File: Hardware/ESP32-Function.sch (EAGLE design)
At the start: 34 parts, among them J1 MICROMOD_STANDARD, Q2 MBT3904DW1T1, U1 EEPROM, U2 ESP-WROOM-3232D-NARROW, U3 3.3V, U4 CP210X

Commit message: Moves to 0603 components where able, adds silk, fixes traces affected by move to 0603
* removes wire stubs
* Fixes random air wires
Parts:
- removed C5: 0.1uF, SparkFun-Capacitors:0.1UF-0402T-16V-10%
- C1: device SparkFun-Capacitors:0.1UF-0402T-16V-10% -> SparkFun-Capacitors:0.1UF-0603-25V-(+80/-20%)
- C4: value 0.1uF -> 1.0uF; device SparkFun-Capacitors:0.1UF-0402T-16V-10% -> SparkFun-Capacitors:1.0UF-0603-16V-10%
- C6: device SparkFun-Capacitors:1.0UF-0402T-16V-10% -> SparkFun-Capacitors:1.0UF-0603-16V-10%
- D1: device SparkFun-MicroMod-Function:LED-0603_RIGHT_ANGLE -> SparkFun-LED:LED-RED0603
- R1, R17, R18, R2: device SparkFun-Resistors:10KOHM-0402T-1/16W-1% -> SparkFun-Resistors:10KOHM-0603-1/10W-1%
- R12: device SparkFun-Resistors:100KOHM-0402T-1/16W-1% -> SparkFun-Resistors:100KOHM-0603-1/10W-1%
- R3, R4: device SparkFun-Resistors:5.1KOHM-0402T-1/16W-1% -> SparkFun-Resistors:5.1KOHM5.1KOHM-0603-1/10W-1%
- R5: device SparkFun-Resistors:22KOHM-0402_TIGHT-1/10W-1% -> SparkFun-Resistors:22KOHM-0603-1/10W-1%
- R6: device SparkFun-Resistors:33KOHM-0402T-1/16W-1% -> SparkFun-Resistors:33KOHM-0603-1/10W-1%
- R7: device SparkFun-Resistors:1KOHM-0402T-1/16W-1% -> SparkFun-Resistors:1KOHM-0603-1/10W-1%
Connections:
- net 3.3V: no longer C5.2
- net GND: no longer C5.1
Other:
- note added: "v10"
- note removed: "v01"
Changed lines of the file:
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@@
 <?xml version="1.0" encoding="utf-8"?>
 <!DOCTYPE eagle SYSTEM "eagle.dtd">
-<eagle version="9.5.1">
+<eagle version="9.6.2">
 <drawing>
 <settings>
@@
 <part name="FD2" library="SparkFun-Aesthetics" deviceset="FIDUCIAL" device="1X2"/>
 <part name="FD4" library="SparkFun-Aesthetics" deviceset="FIDUCIAL" device="1X2"/>
-<part name="R17" library="SparkFun-Resistors" deviceset="10KOHM" device="-0402T-1/16W-1%" value="10k"/>
-<part name="R18" library="SparkFun-Resistors" deviceset="10KOHM" device="-0402T-1/16W-1%" value="10k"/>
+<part name="R17" library="SparkFun-Resistors" deviceset="10KOHM" device="-0603-1/10W-1%" value="10k"/>
+<part name="R18" library="SparkFun-Resistors" deviceset="10KOHM" device="-0603-1/10W-1%" value="10k"/>
 <part name="Q2" library="SparkFun-DiscreteSemi" deviceset="TRANS_NPN_DUAL" device="-MBT3904DW1T1" value="MBT3904DW1T1"/>
-<part name="C4" library="SparkFun-Capacitors" deviceset="0.1UF" device="-0402T-16V-10%" value="0.1uF"/>
+<part name="C4" library="SparkFun-Capacitors" deviceset="1.0UF" device="-0603-16V-10%" value="1.0uF"/>
 <part name="GND11" library="SparkFun-PowerSymbols" deviceset="GND" device=""/>
-<part name="C5" library="SparkFun-Capacitors" deviceset="0.1UF" device="-0402T-16V-10%" value="0.1uF"/>
-<part name="GND13" library="SparkFun-PowerSymbols" deviceset="GND" device=""/>
 <part name="U3" library="SparkFun-IC-Power" deviceset="V_REG_AP2112" device="K-3.3V" value="3.3V"/>
 <part name="GND14" library="SparkFun-PowerSymbols" deviceset="GND" device=""/>
-<part name="C6" library="SparkFun-Capacitors" deviceset="1.0UF" device="-0402T-16V-10%" value="1.0uF"/>
+<part name="C6" library="SparkFun-Capacitors" deviceset="1.0UF" device="-0603-16V-10%" value="1.0uF"/>
 <part name="SUPPLY4" library="SparkFun-PowerSymbols" deviceset="3.3V" device=""/>
-<part name="R12" library="SparkFun-Resistors" deviceset="100KOHM" device="-0402T-1/16W-1%" value="100k"/>
+<part name="R12" library="SparkFun-Resistors" deviceset="100KOHM" device="-0603-1/10W-1%" value="100k"/>
 <part name="SUPPLY5" library="SparkFun-PowerSymbols" deviceset="VCC" device=""/>
 <part name="SUPPLY7" library="SparkFun-PowerSymbols" deviceset="VCC" device=""/>
@@
 <part name="J1" library="SparkFun-MicroMod-Function" deviceset="MICROMOD" device="_STANDARD" value="MICROMOD_STANDARD"/>
 <part name="GND1" library="SparkFun-PowerSymbols" deviceset="GND" device=""/>
-<part name="R2" library="SparkFun-Resistors" deviceset="10KOHM" device="-0402T-1/16W-1%" value="10k"/>
+<part name="R2" library="SparkFun-Resistors" deviceset="10KOHM" device="-0603-1/10W-1%" value="10k"/>
 <part name="SUPPLY6" library="SparkFun-Aesthetics" deviceset="3.3V" device=""/>
 <part name="GND8" library="SparkFun-Aesthetics" deviceset="GND" device=""/>
@@
 <part name="GND26" library="SparkFun-Aesthetics" deviceset="GND" device=""/>
 <part name="U4" library="SparkFun-IC-Comms" deviceset="CP2102N" device="" value="CP210X"/>
-<part name="R1" library="SparkFun-Resistors" deviceset="10KOHM" device="-0402T-1/16W-1%" value="10k"/>
+<part name="R1" library="SparkFun-Resistors" deviceset="10KOHM" device="-0603-1/10W-1%" value="10k"/>
 <part name="SUPPLY9" library="SparkFun-PowerSymbols" deviceset="3.3V" device=""/>
 <part name="GND7" library="SparkFun-Aesthetics" deviceset="GND" device=""/>
 <part name="J3" library="SparkFun-Connectors" deviceset="USB_C" device="_2-LAYER_PADS"/>
-<part name="R3" library="SparkFun-Resistors" deviceset="5.1KOHM" device="-0402T-1/16W-1%" value="5.1k"/>
-<part name="R4" library="SparkFun-Resistors" deviceset="5.1KOHM" device="-0402T-1/16W-1%" value="5.1k"/>
+<part name="R3" library="SparkFun-Resistors" deviceset="5.1KOHM" device="5.1KOHM-0603-1/10W-1%" value="5.1k"/>
+<part name="R4" library="SparkFun-Resistors" deviceset="5.1KOHM" device="5.1KOHM-0603-1/10W-1%" value="5.1k"/>
 <part name="LOGO2" library="SparkFun-Aesthetics" deviceset="SFE_LOGO_NAME_FLAME" device=".2_INCH"/>
 <part name="LOGO3" library="SparkFun-Aesthetics" deviceset="OSHW-LOGO" device="S"/>
 <part name="S2" library="SparkFun-Switches" deviceset="MOMENTARY-SWITCH-SPST" device="-SMD-5.2MM-TALL"/>
 <part name="GND5" library="SparkFun-Aesthetics" deviceset="GND" device=""/>
-<part name="C1" library="SparkFun-Capacitors" deviceset="0.1UF" device="-0402T-16V-10%" value="0.1uF"/>
+<part name="C1" library="SparkFun-Capacitors" deviceset="0.1UF" device="-0603-25V-(+80/-20%)" value="0.1uF"/>
 <part name="GND6" library="SparkFun-Aesthetics" deviceset="GND" device=""/>
-<part name="R5" library="SparkFun-Resistors" deviceset="22KOHM" device="-0402_TIGHT-1/10W-1%" value="22k"/>
-<part name="R6" library="SparkFun-Resistors" deviceset="33KOHM" device="-0402T-1/16W-1%" value="33k"/>
-<part name="R7" library="SparkFun-Resistors" deviceset="1KOHM" device="-0402T-1/16W-1%" value="1k"/>
-<part name="D1" library="SparkFun-MicroMod-Function" deviceset="LED-0603_RIGHT_ANGLE" device="" value="RED"/>
+<part name="R5" library="SparkFun-Resistors" deviceset="22KOHM" device="-0603-1/10W-1%" value="22k"/>
+<part name="R6" library="SparkFun-Resistors" deviceset="33KOHM" device="-0603-1/10W-1%" value="33k"/>
+<part name="R7" library="SparkFun-Resistors" deviceset="1KOHM" device="-0603-1/10W-1%" value="1k"/>
+<part name="D1" library="SparkFun-LED" deviceset="LED-RED" device="0603" value="RED"/>
 <part name="GND10" library="SparkFun-Aesthetics" deviceset="GND" device=""/>
 <part name="JP1" library="SparkFun-Jumpers" deviceset="JUMPER-SMT_2_NC_TRACE" device="_SILK" package3d_urn="urn:adsk.eagle:package:39281/1" value="JUMPER-SMT_2_NC_TRACE_SILK"/>
@@
 <plain>
 <text x="349.504" y="11.176" size="2.54" layer="94" font="vector">Elias Santistevan</text>
-<text x="424.18" y="7.62" size="2.54" layer="94" font="vector" align="center">v01</text>
+<text x="424.18" y="7.62" size="2.54" layer="94" font="vector" align="center">v10</text>
 <text x="195.58" y="238.76" size="1.905" layer="97" font="vector">Boot Mode Configuration
 Pin        Default     Boot   Download
@@
 <attribute name="VALUE" x="82.804" y="223.901" size="1.778" layer="96" font="vector"/>
 </instance>
-<instance part="GND11" gate="1" x="81.28" y="200.66" smashed="yes">
-<attribute name="VALUE" x="78.74" y="198.12" size="1.778" layer="96" font="vector"/>
-</instance>
-<instance part="C5" gate="G$1" x="91.44" y="228.6" smashed="yes" rot="R180">
-<attribute name="NAME" x="92.456" y="228.727" size="1.778" layer="95" font="vector"/>
-<attribute name="VALUE" x="92.456" y="224.409" size="1.778" layer="96" font="vector"/>
-</instance>
-<instance part="GND13" gate="1" x="91.44" y="200.66" smashed="yes">
-<attribute name="VALUE" x="88.9" y="198.12" size="1.778" layer="96" font="vector"/>
+<instance part="GND11" gate="1" x="81.28" y="208.28" smashed="yes">
+<attribute name="VALUE" x="78.74" y="205.74" size="1.778" layer="96" font="vector"/>
 </instance>
 <instance part="U3" gate="G$1" x="68.58" y="228.6" smashed="yes">
@@
 <attribute name="VALUE" x="60.96" y="220.726" size="1.778" layer="96" font="vector" align="top-left"/>
 </instance>
-<instance part="GND14" gate="1" x="55.88" y="200.66" smashed="yes">
-<attribute name="VALUE" x="53.34" y="198.12" size="1.778" layer="96" font="vector"/>
+<instance part="GND14" gate="1" x="55.88" y="208.28" smashed="yes">
+<attribute name="VALUE" x="53.34" y="205.74" size="1.778" layer="96" font="vector"/>
 </instance>
 <instance part="C6" gate="G$1" x="50.8" y="218.44" smashed="yes">
@@
 <attribute name="VALUE" x="42.164" y="216.281" size="1.778" layer="96" font="vector"/>
 </instance>
-<instance part="SUPPLY4" gate="G$1" x="91.44" y="236.22" smashed="yes">
-<attribute name="VALUE" x="91.44" y="239.014" size="1.778" layer="96" font="vector" align="bottom-center"/>
+<instance part="SUPPLY4" gate="G$1" x="81.28" y="236.22" smashed="yes">
+<attribute name="VALUE" x="81.28" y="239.014" size="1.778" layer="96" font="vector" align="bottom-center"/>
 </instance>
 <instance part="R12" gate="G$1" x="48.26" y="241.3" smashed="yes" rot="R90">
@@
 <segment>
 <wire x1="76.2" y1="233.68" x2="81.28" y2="233.68" width="0.1524" layer="91"/>
-<wire x1="81.28" y1="233.68" x2="91.44" y2="233.68" width="0.1524" layer="91"/>
 <wire x1="81.28" y1="233.68" x2="81.28" y2="231.14" width="0.1524" layer="91"/>
-<wire x1="91.44" y1="231.14" x2="91.44" y2="233.68" width="0.1524" layer="91"/>
 <junction x="81.28" y="233.68"/>
 <pinref part="U3" gate="G$1" pin="OUT"/>
 <pinref part="C4" gate="G$1" pin="1"/>
-<pinref part="C5" gate="G$1" pin="2"/>
 <pinref part="SUPPLY4" gate="G$1" pin="3.3V"/>
-<wire x1="91.44" y1="236.22" x2="91.44" y2="233.68" width="0.1524" layer="91"/>
-<junction x="91.44" y="233.68"/>
+<wire x1="81.28" y1="236.22" x2="81.28" y2="233.68" width="0.1524" layer="91"/>
 </segment>
 <segment>
@@
 <net name="GND" class="0">
 <segment>
-<wire x1="81.28" y1="203.2" x2="81.28" y2="223.52" width="0.1524" layer="91"/>
+<wire x1="81.28" y1="210.82" x2="81.28" y2="223.52" width="0.1524" layer="91"/>
 <pinref part="C4" gate="G$1" pin="2"/>
 <pinref part="GND11" gate="1" pin="GND"/>
-</segment>
-<segment>
-<wire x1="91.44" y1="203.2" x2="91.44" y2="223.52" width="0.1524" layer="91"/>
-<pinref part="C5" gate="G$1" pin="1"/>
-<pinref part="GND13" gate="1" pin="GND"/>
 </segment>
 <segment>
@@
 <pinref part="GND14" gate="1" pin="GND"/>
 <pinref part="C6" gate="G$1" pin="2"/>
-<wire x1="55.88" y1="213.36" x2="55.88" y2="203.2" width="0.1524" layer="91"/>
+<wire x1="55.88" y1="213.36" x2="55.88" y2="210.82" width="0.1524" layer="91"/>
 <wire x1="50.8" y1="213.36" x2="50.8" y2="215.9" width="0.1524" layer="91"/>
 <wire x1="50.8" y1="213.36" x2="55.88" y2="213.36" width="0.1524" layer="91"/>

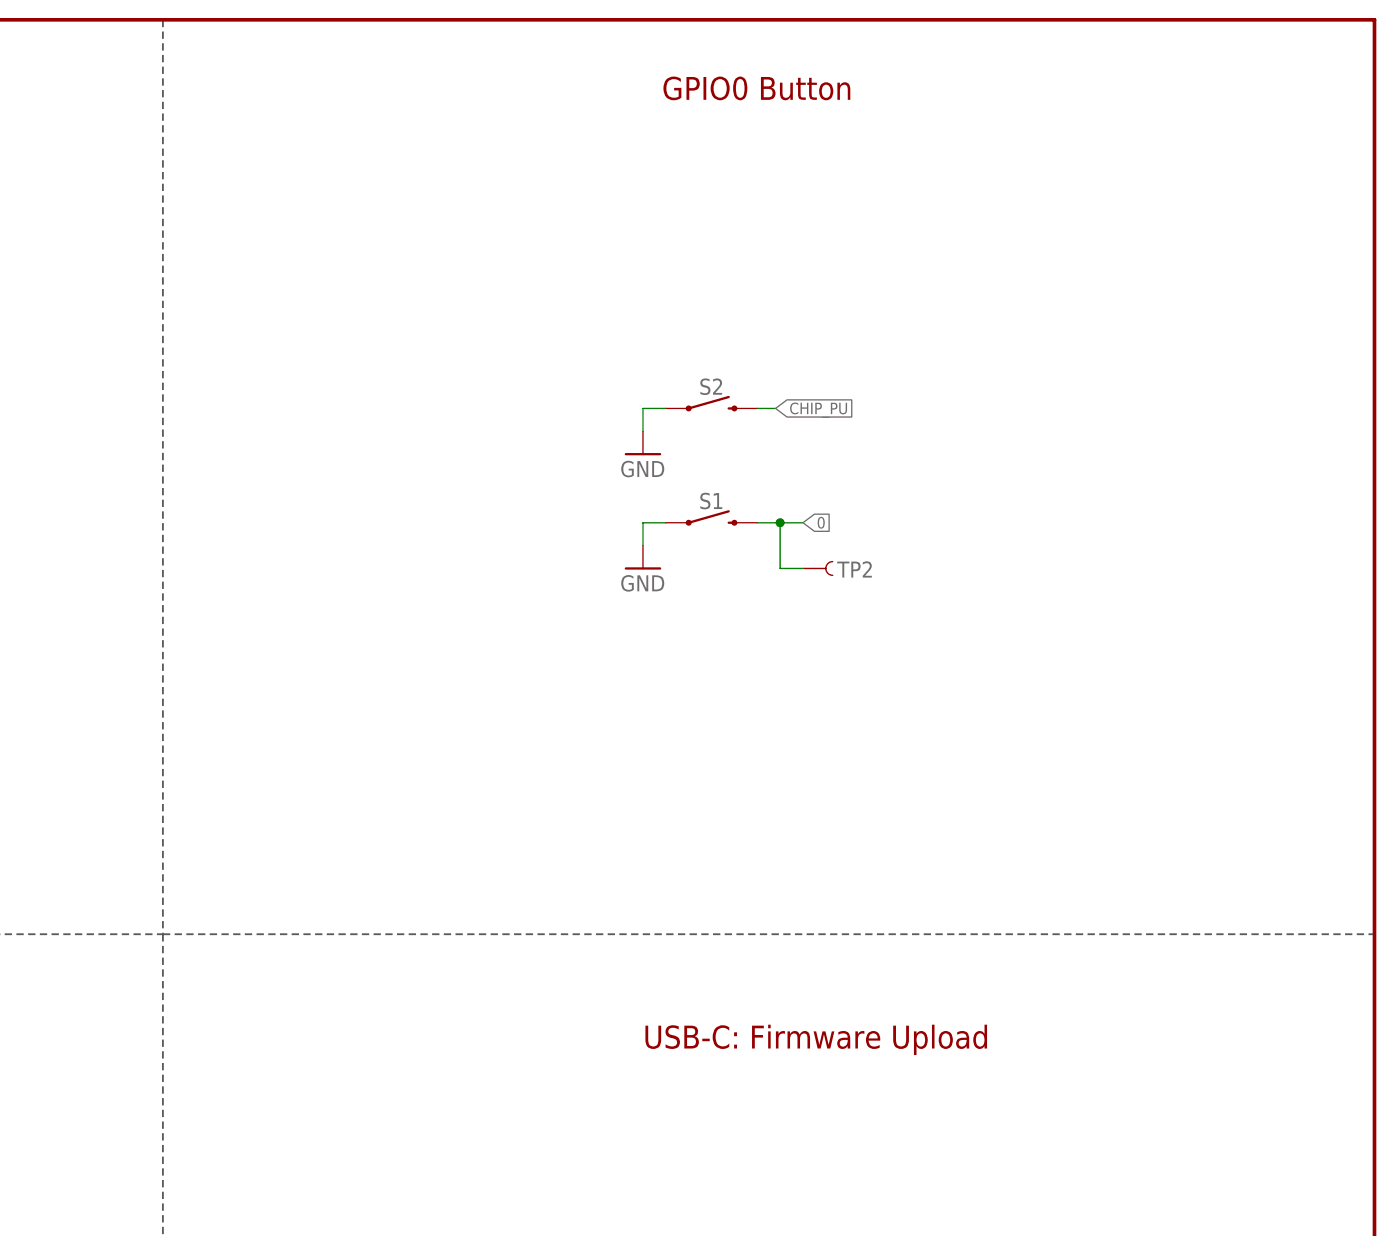
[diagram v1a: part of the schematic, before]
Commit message: Adds I2C pullups and jumper to remove them, rearranges silk
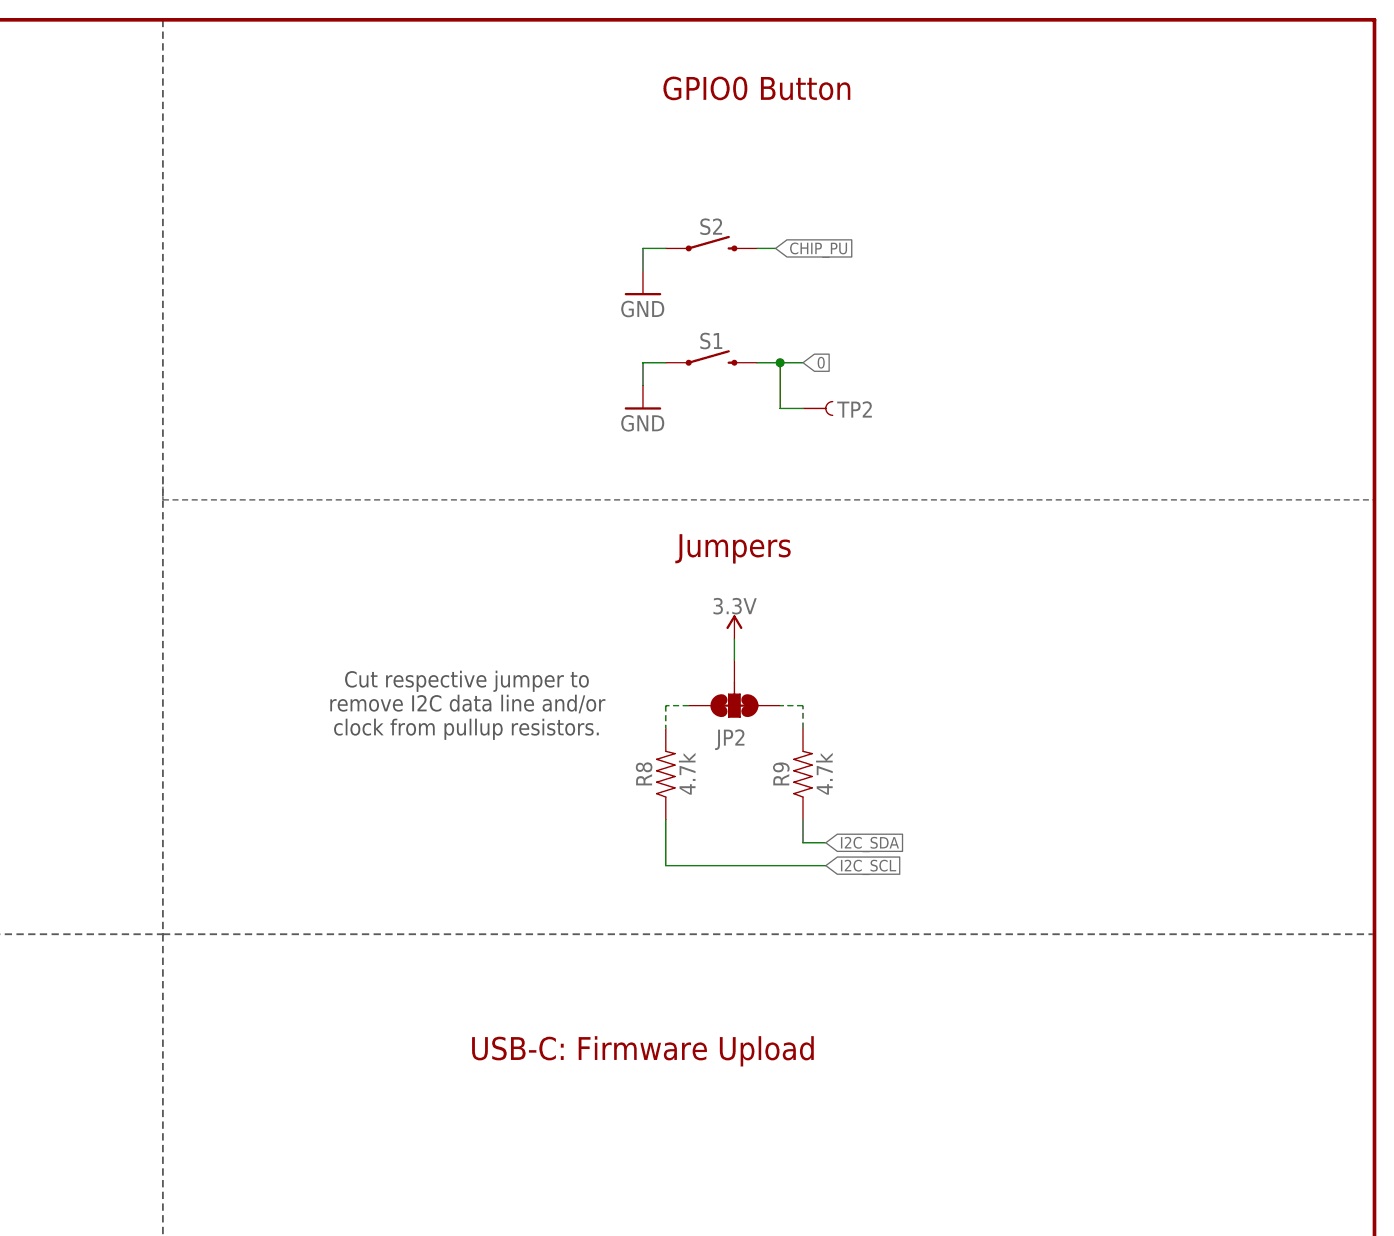
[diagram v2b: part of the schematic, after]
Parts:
- added JP2: JUMPER-SMT_3_2-NC_TRACE_SILK, SparkFun-Jumpers:JUMPER-SMT_3_2-NC_TRACE_SILK
- added R8, R9: 4.7k, SparkFun-Resistors:4.7KOHM-0603-1/10W-1%
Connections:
- new net N$13: JP2.1, R9.2
- new net N$14: JP2.3, R8.2
- net 3.3V: now also JP2.2
- net I2C_SCL: now also R8.1
- net I2C_SDA: now also R9.1
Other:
- note added: "Cut respective jumper to remove I2C data line and/or clock from pullup resistors."
- note added: "Jumpers"
- moved on the sheet: S1, S2, TP2
